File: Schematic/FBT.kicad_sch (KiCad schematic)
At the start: 15 parts, among them J1 Battery, J2 Conn_01x04, J3 Conn_01x04, SW1 SW_SPDT, SW2 SW_SPDT

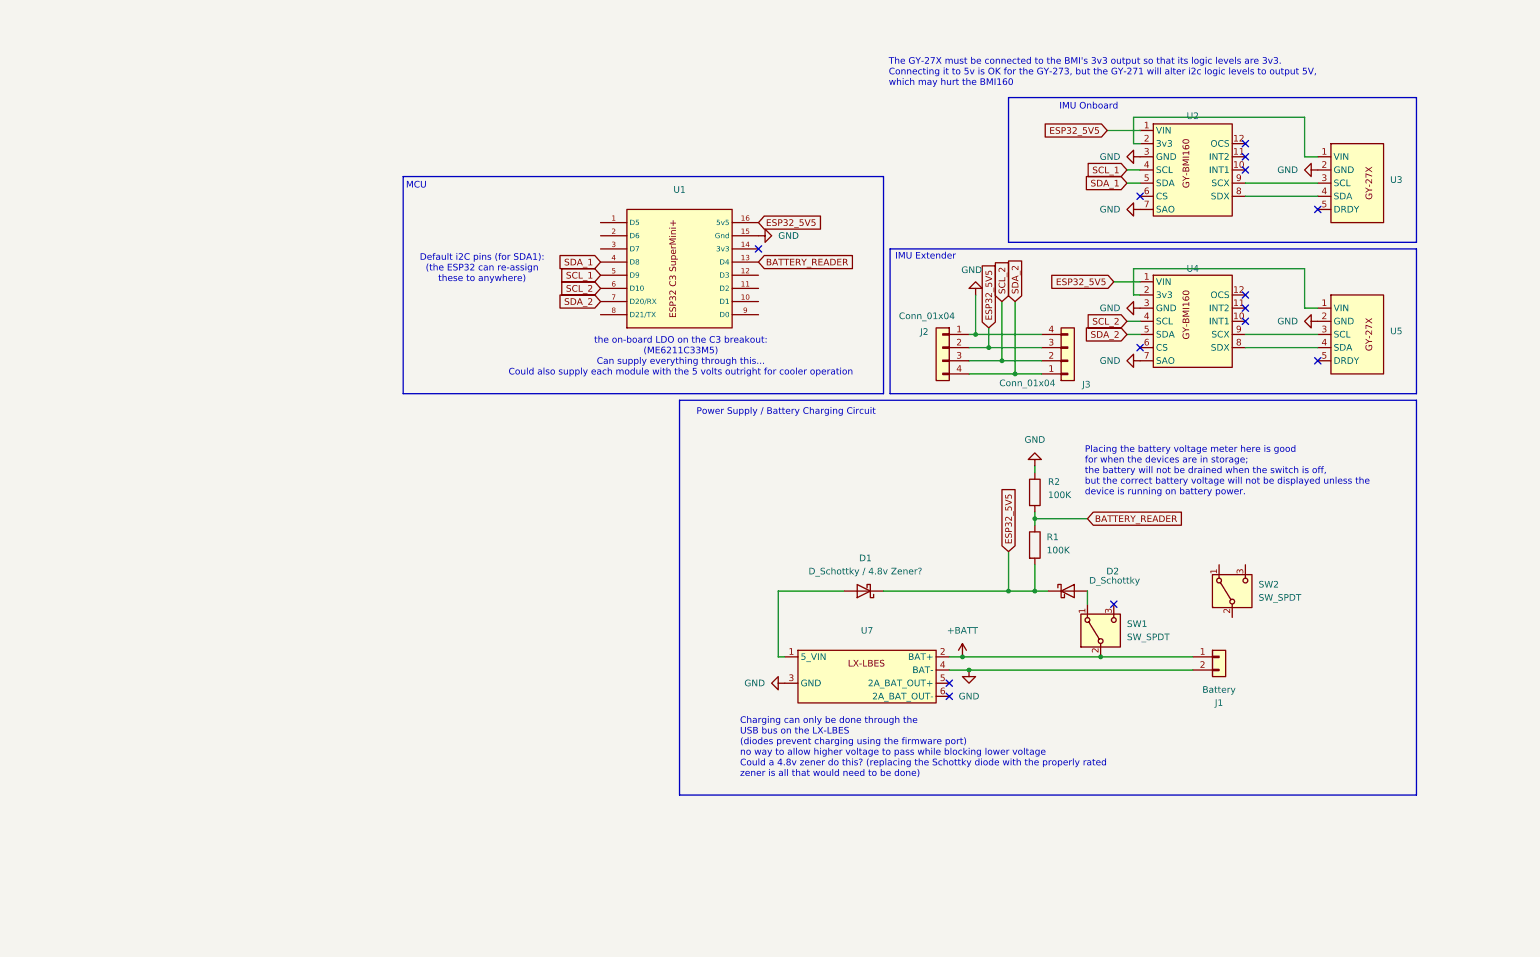
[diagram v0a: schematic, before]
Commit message: More schematic work
I'm kind of hung up on what charging circuit to use...
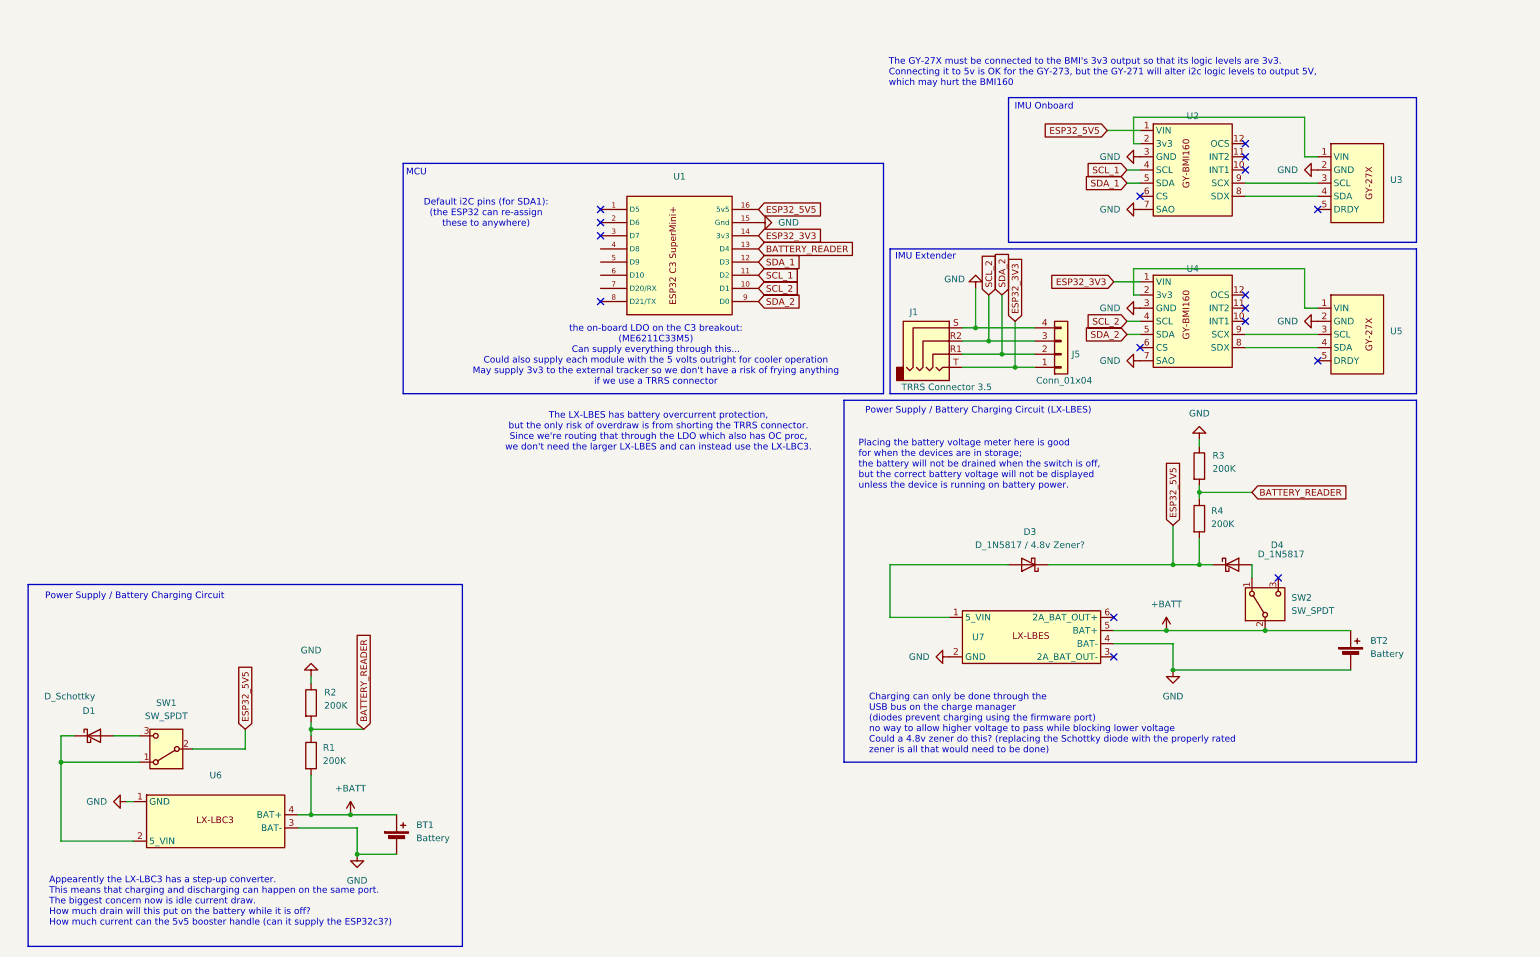
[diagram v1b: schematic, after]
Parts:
- removed D2: D_Schottky, Diode_THT:D_DO-41_SOD81_P7.62mm_Horizontal, symbol Device:D_Schottky
- removed J1: Battery, Connector_JST:JST_XH_B2B-XH-A_1x02_P2.50mm_Vertical, symbol Connector_Generic:Conn_01x02
- removed J2, J3: Conn_01x04, Connector_JST:JST_XH_S4B-XH-A-1_1x04_P2.50mm_Horizontal, symbol Connector_Generic:Conn_01x04
- added BT1, BT2: Battery, Connector_JST:JST_XH_B2B-XH-A_1x02_P2.50mm_Vertical, symbol Device:Battery_Cell
- added D3: D_1N5817 / 4.8v Zener?, Diode_THT:D_DO-41_SOD81_P7.62mm_Horizontal, symbol Device:D_Schottky
- added D4: D_1N5817, Diode_THT:D_DO-41_SOD81_P7.62mm_Horizontal, symbol Device:D_Schottky
- added J1: TRRS Connector 3.5, My_Library:PJ-320A, symbol Connector_Audio:AudioJack4
- added J5: Conn_01x04, Connector_JST:JST_PH_S4B-PH-K_1x04_P2.00mm_Horizontal, symbol Connector_Generic:Conn_01x04
- added R3, R4: 200K, Resistor_THT:R_Axial_DIN0207_L6.3mm_D2.5mm_P7.62mm_Horizontal, symbol Device:R
- added U6: ~, My_Library:LX-LBC3, symbol My_Library:LX-LBC3
- D1: value D_Schottky / 4.8v Zener? -> D_Schottky
- R1, R2: value 100K -> 200K
- SW1: footprint My_Library:SS12D06 -> My_Library:SS12F21
- U7: footprint (none) -> My_Library:LX_LBES
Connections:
- net +BATT: now also R1.2, SW2.2 (B), U7.5 (BAT+), BT1.1 (+), BT2.1 (+), U6.4 (BAT+); no longer SW1.2 (B), U7.2 (BAT+)
- net BATTERY_READER: now also R3.2, R4.1
- net ESP32_5V5: now also SW1.2 (B), D3.1 (K), D4.1 (K), R4.2; no longer D1.1 (K), R1.2, U4.1 (VIN)
- net GND: now also U7.2 (GND), BT1.2 (-), BT2.2 (-), J1.S, J5.4 (Pin_4), R3.1, U6.1 (GND), U6.3 (BAT-); no longer U7.3 (GND)
- net SCL_1: now also U1.11 (D2); no longer U1.5 (D9)
- net SCL_2: now also U1.10 (D1), J1.R2, J5.3 (Pin_3); no longer U1.6 (D10)
- net SDA_1: now also U1.12 (D3); no longer U1.4 (D8)
- net SDA_2: now also U1.9 (D0), J1.R1, J5.2 (Pin_2); no longer U1.7 (D20/RX)
- net at SW1.1 (A): now also D1.1 (K), U6.2 (5_VIN)
- net at SW1.3 (C): now also D1.2 (A)
- net ESP32_3V3: now reaches U1.14 (3v3)
- net ESP32_3V3: now also U4.1 (VIN), J1.T, J5.1 (Pin_1)
- net at U7.1 (5_VIN): now also D3.2 (A); no longer D1.2 (A)
- net at SW2.1 (A): now also D4.2 (A)
- no-connect marks 14 -> 17
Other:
- note added: "Appearently the LX-LBC3 has a step-up converter. This means that charging and discharging can happen on the same port. The biggest concern now is idle current draw. How much drain will this put on the battery while it is off? How much current can the 5v5 booster handle (can it supply the ESP32c3?)"
- note added: "Charging can only be done through the USB bus on the charge manager (diodes prevent charging using the firmware port) no way to allow higher voltage to pass while blocking lower voltage Could a 4.8v zener do this? (replacing the Schottky diode with the properly rated zener is all that would need to be done)"
- note added: "Power Supply / Battery Charging Circuit (LX-LBES)"
- note added: "The LX-LBES has battery overcurrent protection, but the only risk of overdraw is from shorting the TRRS connector. Since we're routing that through the LDO which also has OC proc, we don't need the larger LX-LBES and can instead use the LX-LBC3."
- note added: "the on-board LDO on the C3 breakout: (ME6211C33M5) Can supply everything through this... Could also supply each module with the 5 volts outright for cooler operation May supply 3v3 to the external tracker so we don't have a risk of frying anything if we use a TRRS connector"
- note removed: "Charging can only be done through the USB bus on the LX-LBES (diodes prevent charging using the firmware port) no way to allow higher voltage to pass while blocking lower voltage Could a 4.8v zener do this? (replacing the Schottky diode with the properly rated zener is all that would need to be done)"
- note removed: "the on-board LDO on the C3 breakout: (ME6211C33M5) Can supply everything through this... Could also supply each module with the 5 volts outright for cooler operation"
- moved on the sheet: R1, R2, SW1, U1, U7

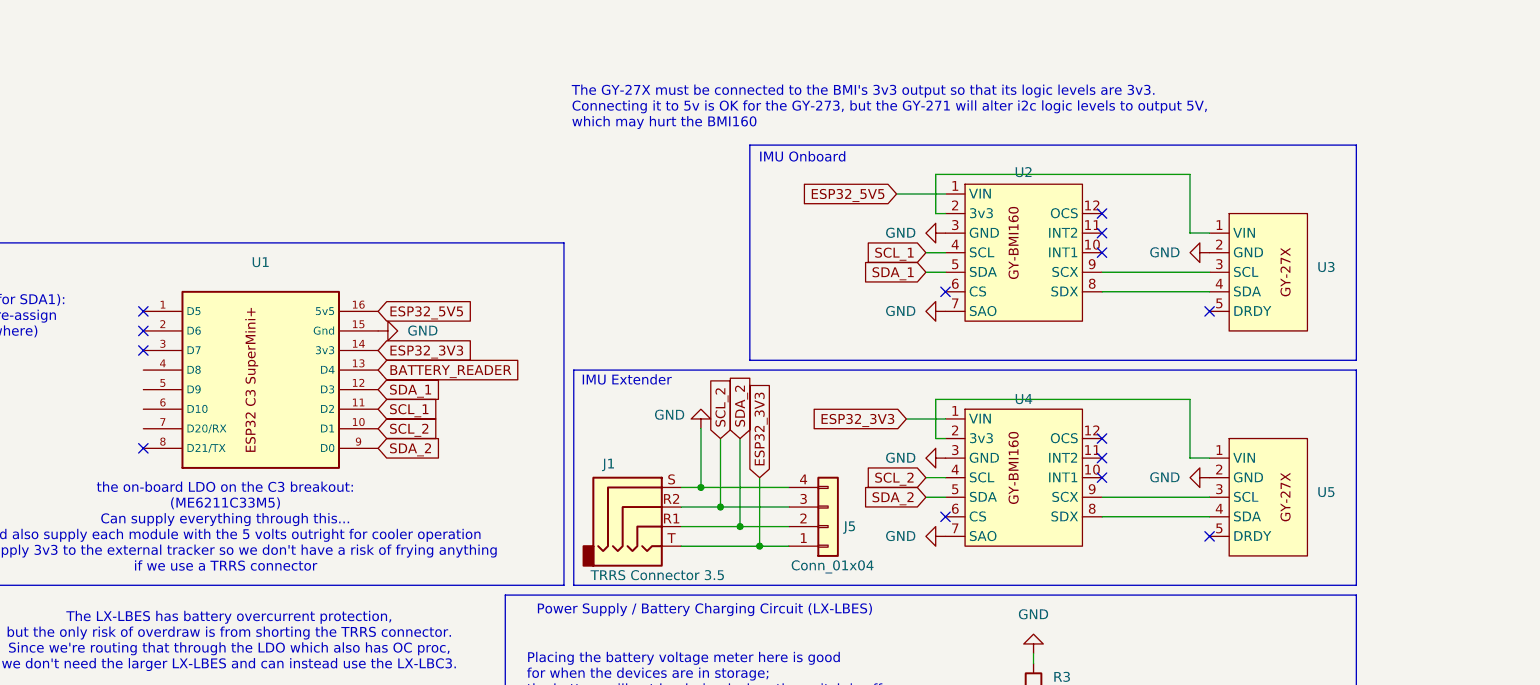
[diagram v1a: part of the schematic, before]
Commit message: Re-work PCB and add more IMU refs
Trying to make this as dynamic as possible
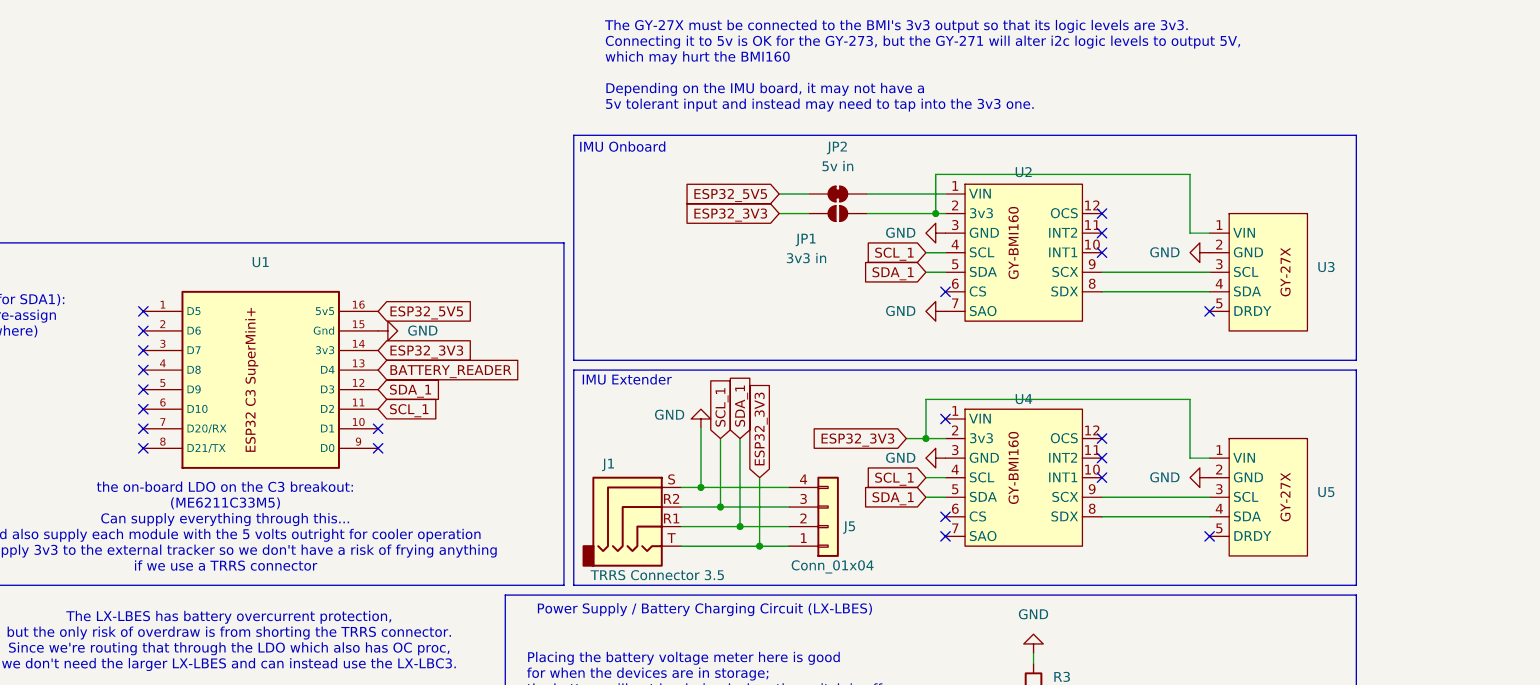
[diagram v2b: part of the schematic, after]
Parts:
- added JP1: 3v3 in, Jumper:SolderJumper-2_P1.3mm_Open_RoundedPad1.0x1.5mm, symbol Jumper:SolderJumper_2_Open
- added JP2: 5v in, Jumper:SolderJumper-2_P1.3mm_Bridged_RoundedPad1.0x1.5mm, symbol Jumper:SolderJumper_2_Bridged
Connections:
- net ESP32_3V3: now also U4.2 (3v3), U5.1 (VIN), JP1.1 (A); no longer U4.1 (VIN)
- net ESP32_5V5: now also JP2.2 (B); no longer U2.1 (VIN)
- net GND: no longer U4.7 (SAO)
- net SCL_1: now also J1.R2, J5.3 (Pin_3), U4.4 (SCL)
- net SDA_1: now also J1.R1, J5.2 (Pin_2), U4.5 (SDA)
- net at U2.2 (3v3), U3.1 (VIN): now also JP1.2 (B)
- removed net SCL_2: J1.R2, J5.3 (Pin_3), U1.10 (D1), U4.4 (SCL)
- removed net SDA_2: J1.R1, J5.2 (Pin_2), U1.9 (D0), U4.5 (SDA)
- new net: JP2.1 (A), U2.1 (VIN)
- no-connect marks 17 -> 25
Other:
- note added: "The GY-27X must be connected to the BMI's 3v3 output so that its logic levels are 3v3. Connecting it to 5v is OK for the GY-273, but the GY-271 will alter i2c logic levels to output 5V, which may hurt the BMI160 Depending on the IMU board, it may not have a 5v tolerant input and instead may need to tap into the 3v3 one."
- note removed: "The GY-27X must be connected to the BMI's 3v3 output so that its logic levels are 3v3. Connecting it to 5v is OK for the GY-273, but the GY-271 will alter i2c logic levels to output 5V, which may hurt the BMI160"

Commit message: schematic work and notes
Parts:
- removed BT1: Battery, Connector_JST:JST_XH_B2B-XH-A_1x02_P2.50mm_Vertical, symbol Device:Battery_Cell
- removed D1: D_Schottky, Diode_THT:D_DO-41_SOD81_P7.62mm_Horizontal, symbol Device:D_Schottky
- removed R1, R2: 200K, Resistor_THT:R_Axial_DIN0207_L6.3mm_D2.5mm_P7.62mm_Horizontal, symbol Device:R
- removed SW1: SW_SPDT, My_Library:SS12F21, symbol Switch:SW_SPDT
- removed U6: ~, My_Library:LX-LBC3, symbol My_Library:LX-LBC3
- JP1: value 3v3 in -> 5v in
- JP2: value 5v in -> 3v3 in
- SW1: renamed from SW2; footprint My_Library:SS12F21 -> My_Library:SK12D07VG4
- renumbered BT2 to BT1, U7 to CHGR1, D3 to D1, D4 to D2, U3 to GY1, U5 to GY2, U2 to IMU1, U4 to IMU2, J5 to J2, U1 to MCU1, R3 to R1, R4 to R2
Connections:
- net ESP32_3V3: now also JP2.1 (A); no longer JP1.1 (A)
- net ESP32_5V5: now also JP1.2 (B); no longer JP2.2 (B)
- net at GY1.1 (VIN), IMU1.2 (3v3): now also JP2.2 (B); no longer JP1.2 (B)
- net at SW1.1 (A): no longer D2.2 (A)
- net at SW1.3 (C): now also D2.2 (A)
- net at IMU1.1 (VIN): now also JP1.1 (A); no longer JP2.1 (A)
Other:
- note removed: "Appearently the LX-LBC3 has a step-up converter. This means that charging and discharging can happen on the same port. The biggest concern now is idle current draw. How much drain will this put on the battery while it is off? How much current can the 5v5 booster handle (can it supply the ESP32c3?)"
- note removed: "Power Supply / Battery Charging Circuit"
- moved on the sheet: JP1, JP2
